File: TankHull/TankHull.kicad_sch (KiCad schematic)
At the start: 64 parts, among them J1 SlipRing_4, J2 Conn_01x02_Socket, J3 Conn_01x02_Socket, J4 Conn_01x02_Socket, J5 Conn_01x02_Socket, J7 Conn_01x05, Q1 Q_PMOS, U10 TSSP77038TR, U11 TSSP77038TR, U12 TSSP77038TR, U2 DRV8833PWP, U3 DRV8833PWP, U4 TSSP77038TR, U5 TSSP77038TR, U6 TSSP77038TR, U7 TSSP77038TR, U8 PCA9555PW, U9 TSSP77038TR

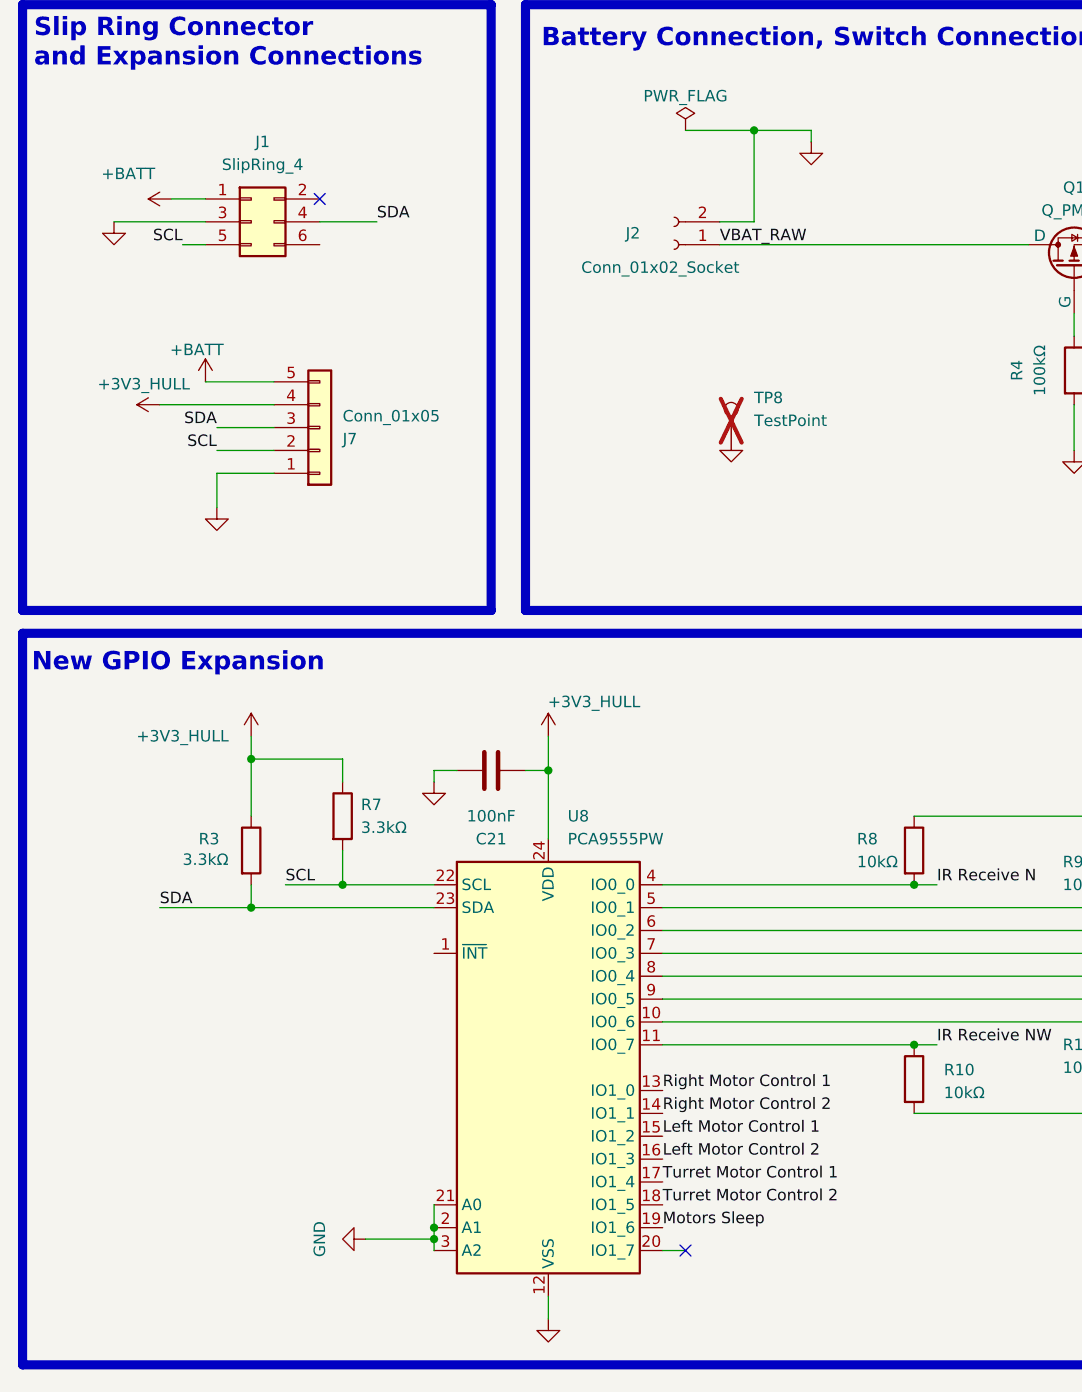
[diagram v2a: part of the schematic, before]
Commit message: continued with IR receiver update
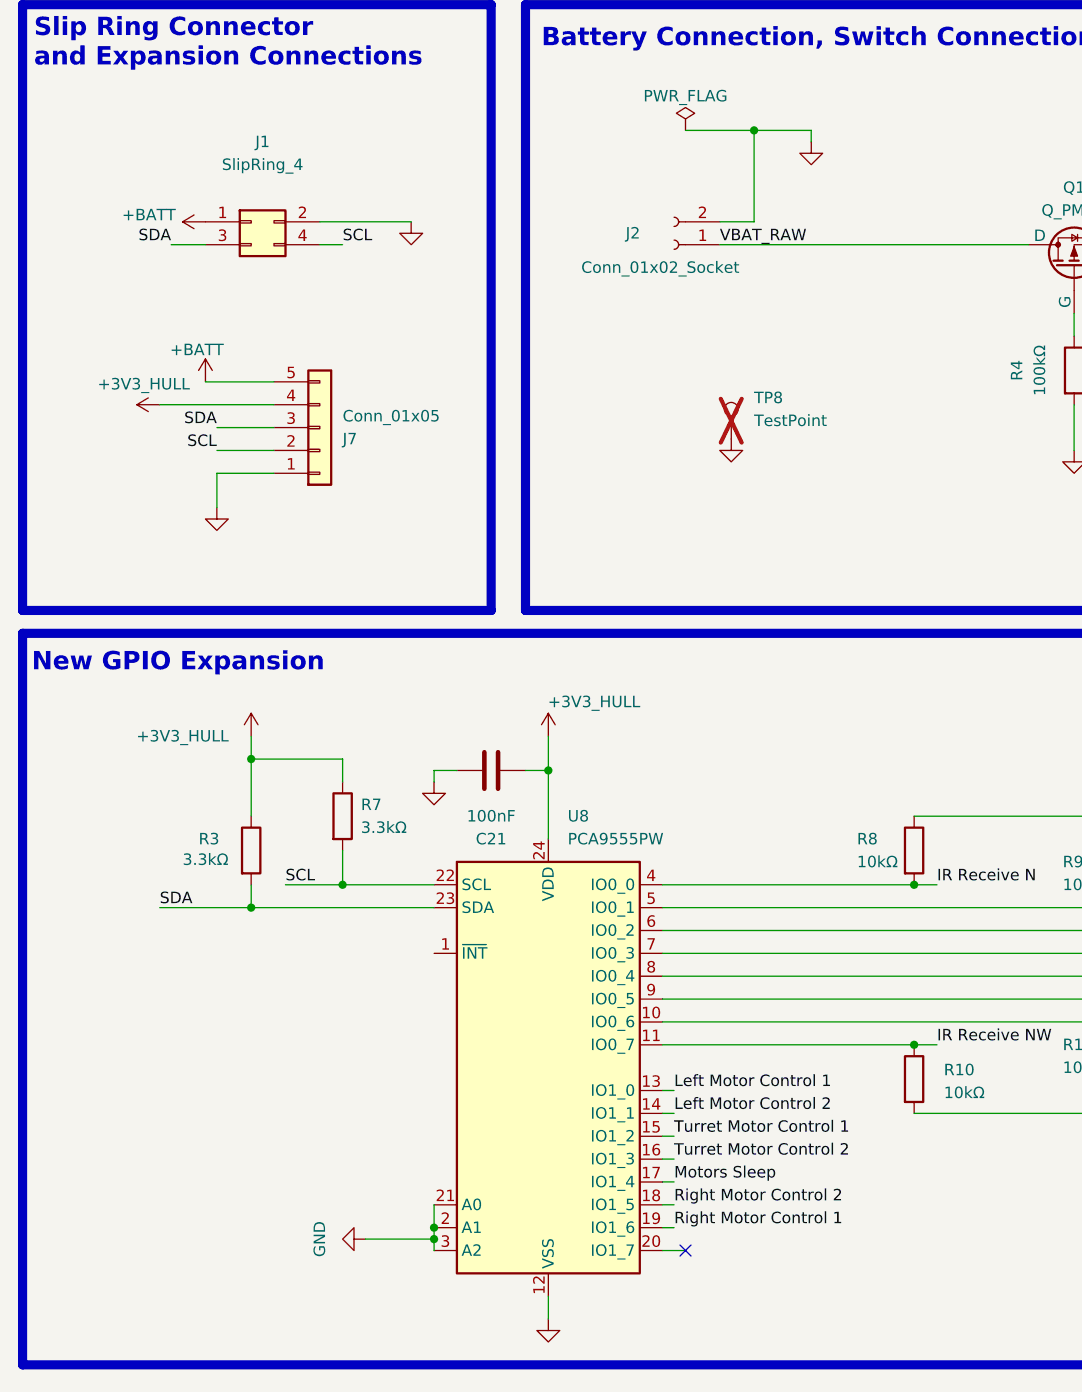
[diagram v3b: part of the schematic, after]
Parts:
- J1: symbol Connector_Generic:Conn_02x03_Odd_Even -> Connector_Generic:Conn_02x02_Odd_Even
- R10, R11, R13, R14, R18, R19, R8, R9: footprint Resistor_SMD:R_0603_1608Metric -> Resistor_SMD:R_01005_0402Metric
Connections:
- net GND: now also J1.2 (Pin_2); no longer J1.3 (Pin_3)
- net Left Motor Control 1: now also U8.13 (IO1_0); no longer U8.15 (IO1_2)
- net Left Motor Control 2: now also U8.14 (IO1_1); no longer U8.16 (IO1_3)
- net Motors Sleep: now also U8.17 (IO1_4); no longer U8.19 (IO1_6)
- net Right Motor Control 1: now also U8.19 (IO1_6); no longer U8.13 (IO1_0)
- net Right Motor Control 2: now also U8.18 (IO1_5); no longer U8.14 (IO1_1)
- net SCL: now also J1.4 (Pin_4); no longer J1.5 (Pin_5)
- net SDA: now also J1.3 (Pin_3); no longer J1.4 (Pin_4)
- net Turret Motor Control 1: now also U8.15 (IO1_2); no longer U8.17 (IO1_4)
- net Turret Motor Control 2: now also U8.16 (IO1_3); no longer U8.18 (IO1_5)
- no-connect marks 8 -> 7
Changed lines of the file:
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@@
 	)
 	(no_connect
-		(at 63.5 46.99)
-	)
-	(no_connect
 		(at 100.33 240.03)
 	)
@@
 	(wire
 		(pts
-			(xy 63.5 49.53) (xy 69.85 49.53)
-		)
-		(stroke
-			(width 0)
-			(type default)
-		)
-	)
-	(wire
-		(pts
 			(xy 328.93 181.61) (xy 345.44 181.61)
 		)
@@
 	(wire
 		(pts
-			(xy 40.64 49.53) (xy 50.8 49.53)
+			(xy 194.31 133.35) (xy 203.2 133.35)
 		)
 		(stroke
@@
 	(wire
 		(pts
-			(xy 194.31 133.35) (xy 203.2 133.35)
+			(xy 76.2 161.29) (xy 76.2 162.56)
 		)
 		(stroke
@@
 	(wire
 		(pts
-			(xy 76.2 161.29) (xy 76.2 162.56)
+			(xy 290.83 81.28) (xy 288.29 81.28)
 		)
 		(stroke
@@
 	(wire
 		(pts
-			(xy 290.83 81.28) (xy 288.29 81.28)
+			(xy 102.87 146.05) (xy 101.6 146.05)
 		)
 		(stroke
@@
 	(wire
 		(pts
+			(xy 102.87 148.59) (xy 101.6 148.59)
+		)
+		(stroke
+			(width 0)
+			(type default)
+		)
+	)
+	(wire
+		(pts
 			(xy 50.8 67.31) (xy 58.42 67.31)
 		)
@@
 	(wire
 		(pts
+			(xy 46.99 52.07) (xy 50.8 52.07)
+		)
+		(stroke
+			(width 0)
+			(type default)
+		)
+	)
+	(wire
+		(pts
 			(xy 345.44 161.29) (xy 353.06 161.29)
 		)
@@
 	(wire
 		(pts
+			(xy 102.87 161.29) (xy 101.6 161.29)
+		)
+		(stroke
+			(width 0)
+			(type default)
+		)
+	)
+	(wire
+		(pts
 			(xy 88.9 106.68) (xy 88.9 110.49)
 		)
@@
 	(wire
 		(pts
+			(xy 102.87 151.13) (xy 101.6 151.13)
+		)
+		(stroke
+			(width 0)
+			(type default)
+		)
+	)
+	(wire
+		(pts
 			(xy 63.5 245.11) (xy 69.85 245.11)
 		)
@@
 	(wire
 		(pts
+			(xy 66.04 52.07) (xy 63.5 52.07)
+		)
+		(stroke
+			(width 0)
+			(type default)
+		)
+	)
+	(wire
+		(pts
 			(xy 76.2 162.56) (xy 76.2 163.83)
 		)
@@
 	(wire
 		(pts
-			(xy 48.26 52.07) (xy 50.8 52.07)
-		)
-		(stroke
-			(width 0)
-			(type default)
-		)
-	)
-	(wire
-		(pts
 			(xy 177.8 209.55) (xy 215.9 209.55)
 		)
@@
 	(wire
 		(pts
-			(xy 46.99 46.99) (xy 50.8 46.99)
-		)
-		(stroke
-			(width 0)
-			(type default)
-		)
-	)
-	(wire
-		(pts
 			(xy 328.93 95.25) (xy 328.93 118.11)
 		)
@@
 	(wire
 		(pts
+			(xy 102.87 153.67) (xy 101.6 153.67)
+		)
+		(stroke
+			(width 0)
+			(type default)
+		)
+	)
+	(wire
+		(pts
 			(xy 328.93 204.47) (xy 345.44 204.47)
 		)
@@
 	(wire
 		(pts
+			(xy 102.87 158.75) (xy 101.6 158.75)
+		)
+		(stroke
+			(width 0)
+			(type default)
+		)
+	)
+	(wire
+		(pts
 			(xy 176.53 148.59) (xy 194.31 148.59)
 		)
@@
 	(wire
 		(pts
+			(xy 73.66 49.53) (xy 63.5 49.53)
+		)
+		(stroke
+			(width 0)
+			(type default)
+		)
+	)
+	(wire
+		(pts
 			(xy 176.53 143.51) (xy 176.53 148.59)
 		)
@@
 	(wire
 		(pts
+			(xy 102.87 156.21) (xy 101.6 156.21)
+		)
+		(stroke
+			(width 0)
+			(type default)
+		)
+	)
+	(wire
+		(pts
 			(xy 43.18 209.55) (xy 43.18 229.87)
 		)
@@
 	)
 	(label "Right Motor Control 2"
-		(at 101.6 148.59 0)
+		(at 102.87 158.75 0)
 		(effects
 			(font
@@
 	)
 	(label "Turret Motor Control 1"
-		(at 101.6 156.21 0)
+		(at 102.87 151.13 0)
 		(effects
 			(font
@@
 	)
 	(label "SCL"
-		(at 48.26 52.07 180)
+		(at 66.04 52.07 0)
 		(effects
 			(font
 				(size 1.27 1.27)
 			)
-			(justify right bottom)
+			(justify left bottom)
 		)
 	)
 	(label "Turret Motor Control 2"
-		(at 101.6 158.75 0)
+		(at 102.87 153.67 0)
 		(effects
 			(font
@@
 	)
 	(label "Right Motor Control 1"
-		(at 101.6 146.05 0)
+		(at 102.87 161.29 0)
 		(effects
 			(font
@@
 	)
 	(label "Left Motor Control 2"
-		(at 101.6 153.67 0)
+		(at 102.87 148.59 0)
 		(effects
 			(font
@@
 	)
 	(label "Motors Sleep"
-		(at 101.6 161.29 0)
+		(at 102.87 156.21 0)
 		(effects
 			(font
@@
 	)
 	(label "SDA"
-		(at 69.85 49.53 0)
+		(at 46.99 52.07 180)
 		(effects
 			(font
 				(size 1.27 1.27)
 			)
-			(justify left bottom)
+			(justify right bottom)
 		)
 	)
@@
 	)
 	(label "Left Motor Control 1"
-		(at 101.6 151.13 0)
+		(at 102.87 146.05 0)
 		(effects
 			(font
@@
 			)
 		)
-		(property "Footprint" "Resistor_SMD:R_0603_1608Metric"
+		(property "Footprint" "Resistor_SMD:R_01005_0402Metric"
 			(at 174.752 124.46 90)
 			(effects
@@
 			)
 		)
-		(property "Footprint" "Resistor_SMD:R_0603_1608Metric"
+		(property "Footprint" "Resistor_SMD:R_01005_0402Metric"
 			(at 127.762 119.38 90)
 			(effects
@@
 			)
 		)
-		(property "Footprint" "Resistor_SMD:R_0603_1608Metric"
+		(property "Footprint" "Resistor_SMD:R_01005_0402Metric"
 			(at 192.532 137.16 90)
 			(effects
@@
 	(symbol
 		(lib_id "power:GND")
-		(at 40.64 49.53 0)
+		(at 73.66 49.53 0)
 		(unit 1)
 		(exclude_from_sim no)
@@
 		(dnp no)
 		(property "Reference" "#PWR03"
-			(at 40.64 55.88 0)
+			(at 73.66 55.88 0)
 			(effects
 				(font
@@
 		)
 		(property "Value" "GND"
-			(at 40.64 54.61 0)
+			(at 73.66 54.61 0)
 			(effects
 				(font
@@
 		)
 		(property "Footprint" ""
-			(at 40.64 49.53 0)
+			(at 73.66 49.53 0)
 			(effects
 				(font
@@
 		)
 		(property "Datasheet" ""
-			(at 40.64 49.53 0)
+			(at 73.66 49.53 0)
 			(effects
 				(font
@@
 		)
 		(property "Description" "Power symbol creates a global label with name \"GND\" , ground"
-			(at 40.64 49.53 0)
+			(at 73.66 49.53 0)
 			(effects
 				(font
@@
 			)
 		)
-		(property "Footprint" "Resistor_SMD:R_0603_1608Metric"
+		(property "Footprint" "Resistor_SMD:R_01005_0402Metric"
 			(at 150.622 142.24 90)
 			(effects
@@
 	)
 	(symbol
-		(lib_id "Connector_Generic:Conn_02x03_Odd_Even")
+		(lib_id "Connector_Generic:Conn_02x02_Odd_Even")
 		(at 55.88 49.53 0)
 		(unit 1)
@@
 			)
 		)
-		(property "Description" "-25℃~+85℃ 1 1x4P 2.5mm 250V 3A 4 4P 5.9mm 7mm Brass PA66 Through Hole Tin UL94V-0 XH Plugin,P=2.5mm Wire To Board Connector ROHS"
+		(property "Description" "Generic connector, double row, 02x02, odd/even pin numbering scheme (row 1 odd numbers, row 2 even numbers), script generated (kicad-library-utils/schlib/autogen/connector/)"
 			(at 55.88 49.53 0)
 			(effects
@@
 		(pin "3"
 		)
-		(pin "5"
-		)
 		(pin "1"
 		)
@@
 		(pin "4"
 		)
-		(pin "6"
-		)
 		(instances
 			(project ""
@@
 			)
 		)
-		(property "Footprint" "Resistor_SMD:R_0603_1608Metric"
+		(property "Footprint" "Resistor_SMD:R_01005_0402Metric"
 			(at 192.532 127 90)
 			(effects
@@
 			)
 		)
-		(property "Footprint" "Resistor_SMD:R_0603_1608Metric"
+		(property "Footprint" "Resistor_SMD:R_01005_0402Metric"
 			(at 127.762 144.78 90)
 			(effects
@@
 			)
 		)
-		(property "Footprint" "Resistor_SMD:R_0603_1608Metric"
+		(property "Footprint" "Resistor_SMD:R_01005_0402Metric"
 			(at 174.752 139.7 90)
 			(effects
@@
 	(symbol
 		(lib_id "power:+BATT")
-		(at 46.99 46.99 90)
+		(at 50.8 49.53 90)
 		(mirror x)
 		(unit 1)
@@
 		(dnp no)
 		(property "Reference" "#PWR04"
-			(at 50.8 46.99 0)
+			(at 54.61 49.53 0)
 			(effects
 				(font
@@
 		)
 		(property "Value" "+BATT"
-			(at 45.212 44.196 90)
+			(at 47.498 48.768 90)
 			(effects
 				(font
@@
 		)
 		(property "Footprint" ""
-			(at 46.99 46.99 0)
+			(at 50.8 49.53 0)
 			(effects
 				(font
@@
 		)
 		(property "Datasheet" ""
-			(at 46.99 46.99 0)
+			(at 50.8 49.53 0)
 			(effects
 				(font
@@
 		)
 		(property "Description" "Power symbol creates a global label with name \"+BATT\""
-			(at 46.99 46.99 0)
+			(at 50.8 49.53 0)
 			(effects
 				(font
@@
 			)
 		)
-		(property "Footprint" "Resistor_SMD:R_0603_1608Metric"
+		(property "Footprint" "Resistor_SMD:R_01005_0402Metric"
 			(at 150.622 121.92 90)
 			(effects
